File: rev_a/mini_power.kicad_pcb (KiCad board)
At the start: 2 copper layers, 4 parts

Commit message: Did initial board layout.
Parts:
- added N3: OSTTC020162, Mini_Power_Rev_A:5MM_TERMINAL_BLOCK_2_POS, F.Cu at (101.6, 147.3)
- added N4: OSTTC020162, Mini_Power_Rev_A:5MM_TERMINAL_BLOCK_2_POS, F.Cu at (112.4, 147.3)
- added N5: OSTTC020162, Mini_Power_Rev_A:5MM_TERMINAL_BLOCK_2_POS, F.Cu at (122.6, 145.4)
- added N6: OSTTC020162, Mini_Power_Rev_A:5MM_TERMINAL_BLOCK_2_POS, F.Cu at (90.8, 147.3)
- added N7: OSTTC020162, Mini_Power_Rev_A:5MM_TERMINAL_BLOCK_2_POS, F.Cu at (80.6, 145.4)
- added Q1: FQP47P06, Mini_Power_Rev_A:TO-220_FET-GDS_Horizontal_LargePads, F.Cu at (105.4, 132.7)
- added Q2: FQP47P06, Mini_Power_Rev_A:TO-220_FET-GDS_Horizontal_LargePads, F.Cu at (97.8, 132.7)
- added R1: MF-R300, Mini_Power_Rev_A:MF_R300, F.Cu at (101.6, 139.1)
- added R2: RESETABLE_FUSE, Mini_Power_Rev_A:MF_R300, F.Cu at (101.6, 127.0)
- added SW1: F-426-0020, Mini_Power_Rev_A:GF_426_0020, F.Cu at (101.6, 117.5)
- G1: moved to B.Cu
- N1: value MS_DATA_HEADER -> MS_DATA_HEADER_POWER
- N2: value MS_PWR_HEADER -> MS_PWR_HEADER_POWER
- moved G1 13.1 mm to (89.5, 132.7)
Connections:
- N1 pad 1: /D0 -> (no net)
- N1 pad 10: /D9 -> (no net)
- N1 pad 11: /D10 -> (no net)
- N1 pad 12: /D11 -> (no net)
- N1 pad 13: /D12 -> (no net)
- N1 pad 14: /D13 -> (no net)
- N1 pad 2: /D1 -> (no net)
- N1 pad 3: /D2 -> (no net)
- N1 pad 4: /D3 -> (no net)
- N1 pad 5: /D4 -> (no net)
- N1 pad 6: /D5 -> (no net)
- N1 pad 7: /D6 -> (no net)
- N1 pad 8: /D7 -> (no net)
- N1 pad 9: /D8 -> (no net)
- N2 pad 10: /A1 -> (no net)
- N2 pad 11: /A2 -> (no net)
- N2 pad 12: /A3 -> (no net)
- N2 pad 13: /A4 -> (no net)
- N2 pad 14: /A5 -> (no net)
- N2 pad 3: /5V -> (no net)
- N2 pad 4: /3V3 -> (no net)
- N2 pad 7: /AREF -> (no net)
- N2 pad 8: /~RESET -> (no net)
- N2 pad 9: /A0 -> (no net)
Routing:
- net /MGND: track 2.54 -> 55.5 mm
- net /LPWR1: track 0.00 -> 36.8 mm
- net /MPWR3: track 0.00 -> 30.4 mm
- net /VIN: track 2.54 -> 31.6 mm
- net /LPWR4: track 0.00 -> 22.4 mm
- net /MPWR: track 2.54 -> 24.5 mm
- net /MPWR1: track 0.00 -> 18.3 mm
- net /GND: track 21.9 -> 31.4 mm
- net /LPWR2: track 0.00 -> 7.68 mm
- net /LPWR3: track 0.00 -> 7.53 mm
- net /MPWR2: track 0.00 -> 4.33 mm
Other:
- board text added: "+"
- board text added: "-"
- board text added: "E-Stop"
- board text added: "LPWR"
- board text added: "Mini_Power"
- board text added: "OFF"
- board text added: "ON"
- board text added: "Power Mini-Shield Rev. A Copyright (c) 2014 - Gramlich"
- board text added: "Rev. A"
- board text removed: "Copyright (c) 2014 by Wayne Gramlich"
- board text removed: "Mini_Template Rev. A 2014Jun25"

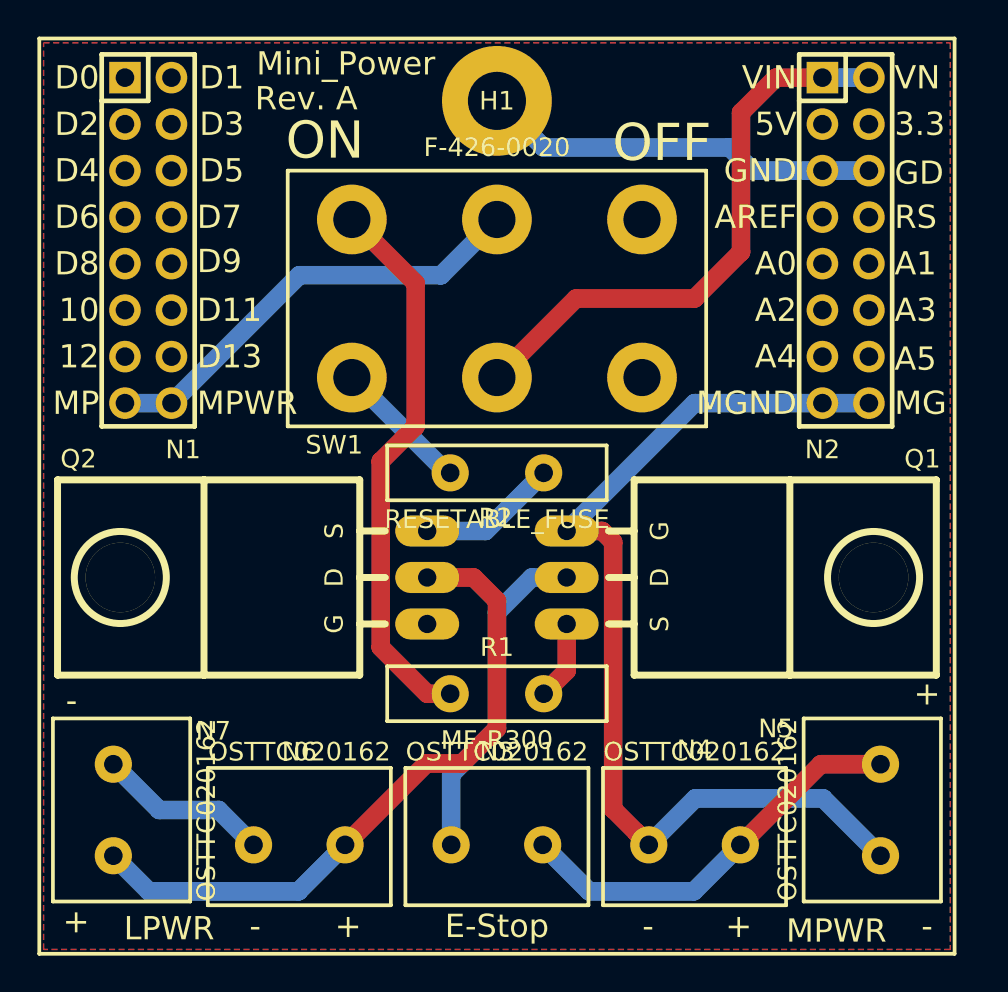
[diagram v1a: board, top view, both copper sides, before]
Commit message: Added Edge Cuts.
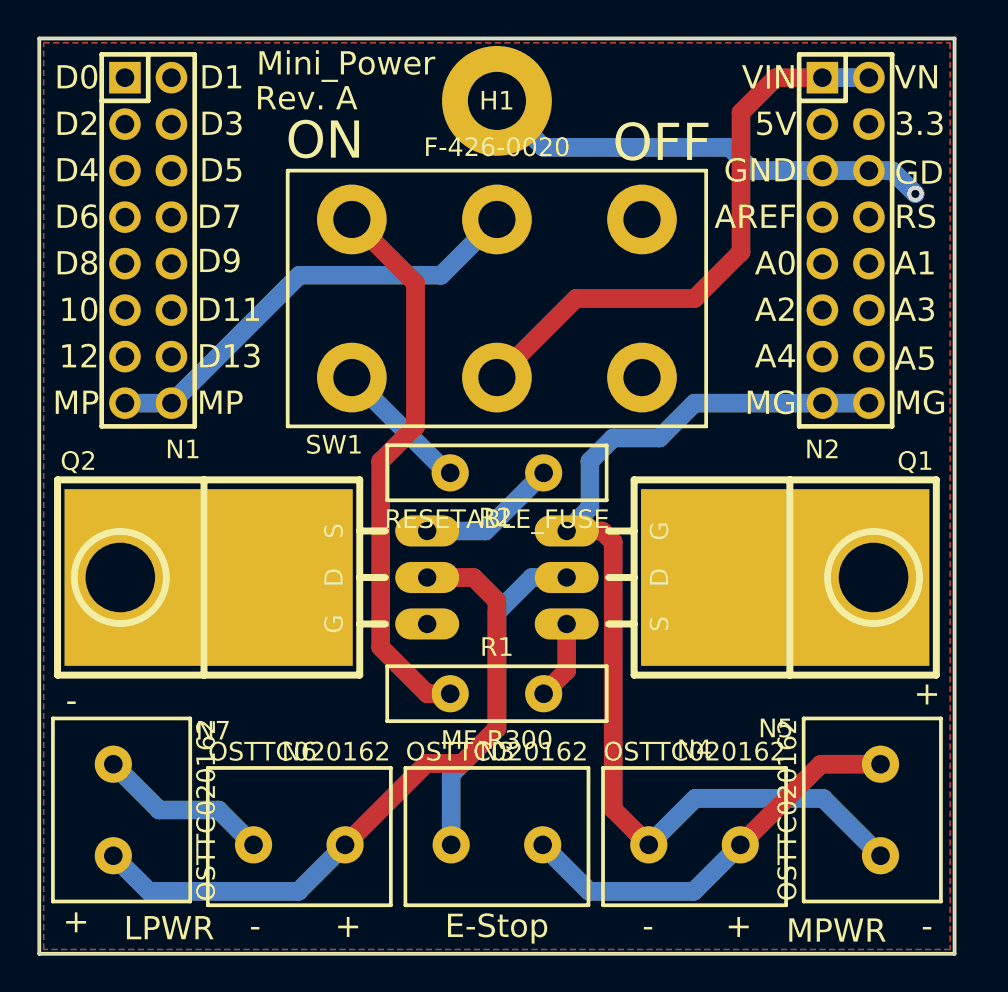
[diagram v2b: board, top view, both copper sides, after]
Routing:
- net /GND: track 31.4 -> 34.4 mm, vias 0 -> 1
- net /MGND: track 55.5 -> 57.0 mm
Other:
- board outline added: 50 x 50 mm
- board text removed: "MGND"
